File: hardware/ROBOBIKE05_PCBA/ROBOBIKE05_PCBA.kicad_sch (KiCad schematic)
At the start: 53 parts, among them J1 3P PIN HEADER, J10 2.54, J11 WIRING HOLE, J2 3P PIN HEADER, J3 3P PIN HEADER, J4 PINHEADER, J5 2.54, J6 SM-2P, J7 SM-2R, J8 2.54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

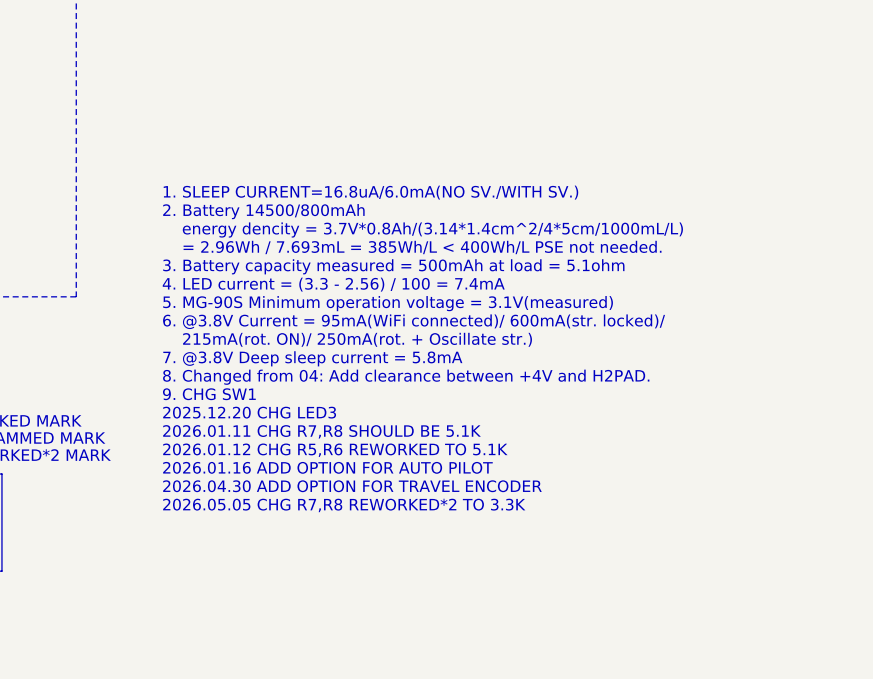
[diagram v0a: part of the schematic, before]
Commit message: diff Lopass coeff chg
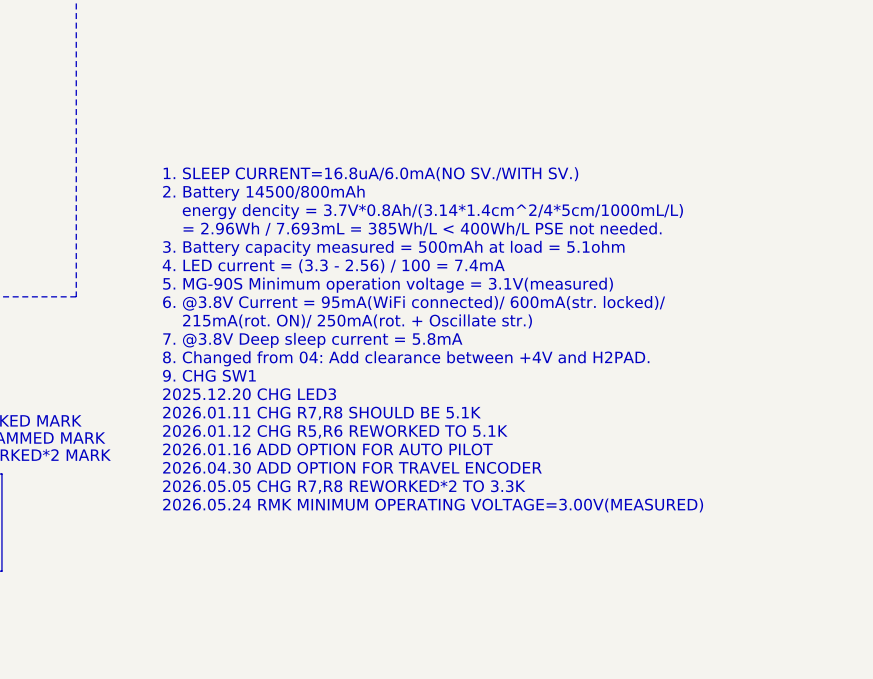
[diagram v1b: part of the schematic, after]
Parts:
- TP1, TP2, TP3: value ~ -> (none)
